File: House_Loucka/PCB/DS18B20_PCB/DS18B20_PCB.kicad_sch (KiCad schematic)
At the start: 3 parts, among them U1 DS18B20, U2 DS18B20, U3 DS18B20

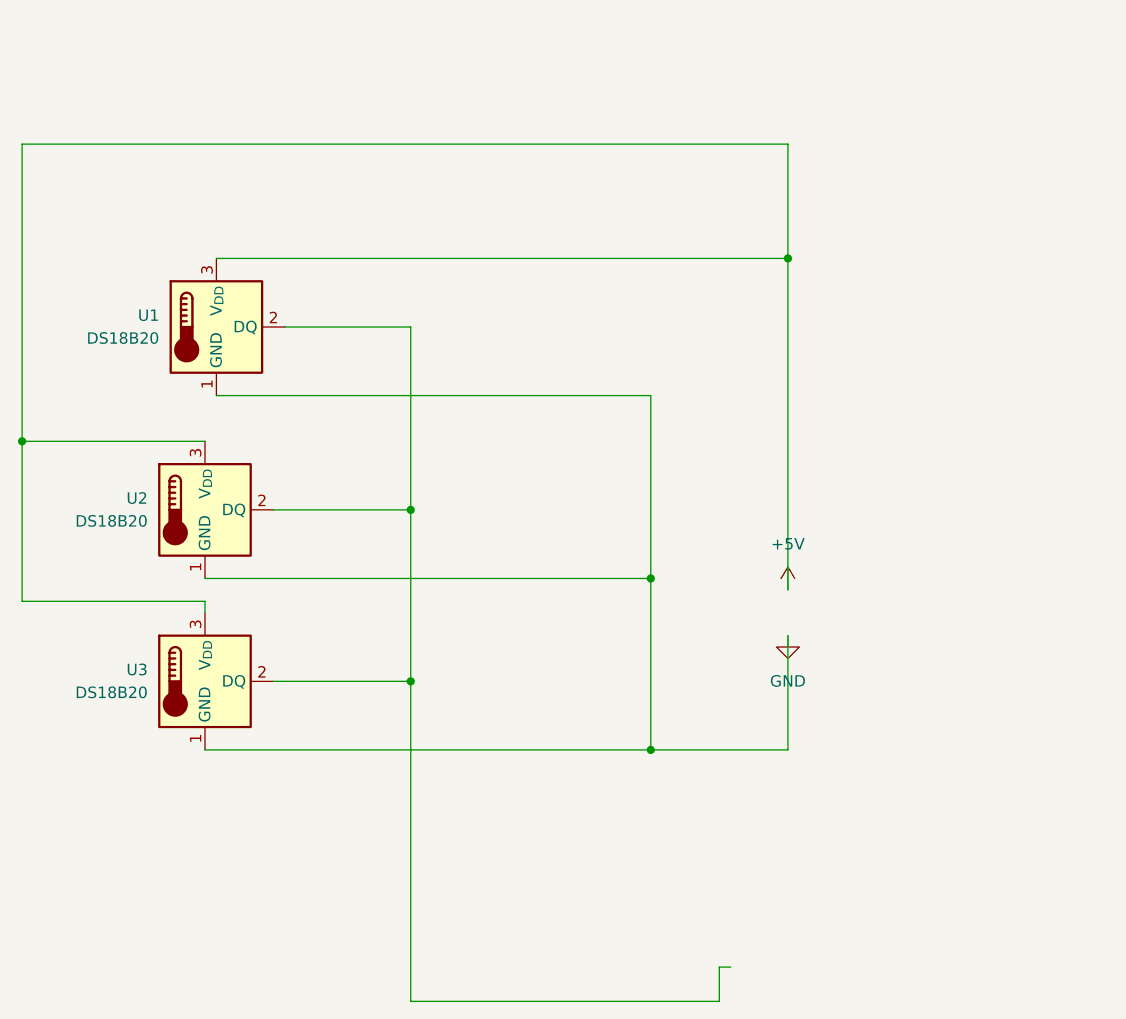
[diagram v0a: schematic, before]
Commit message: Update PCB DS18B20 tables updated
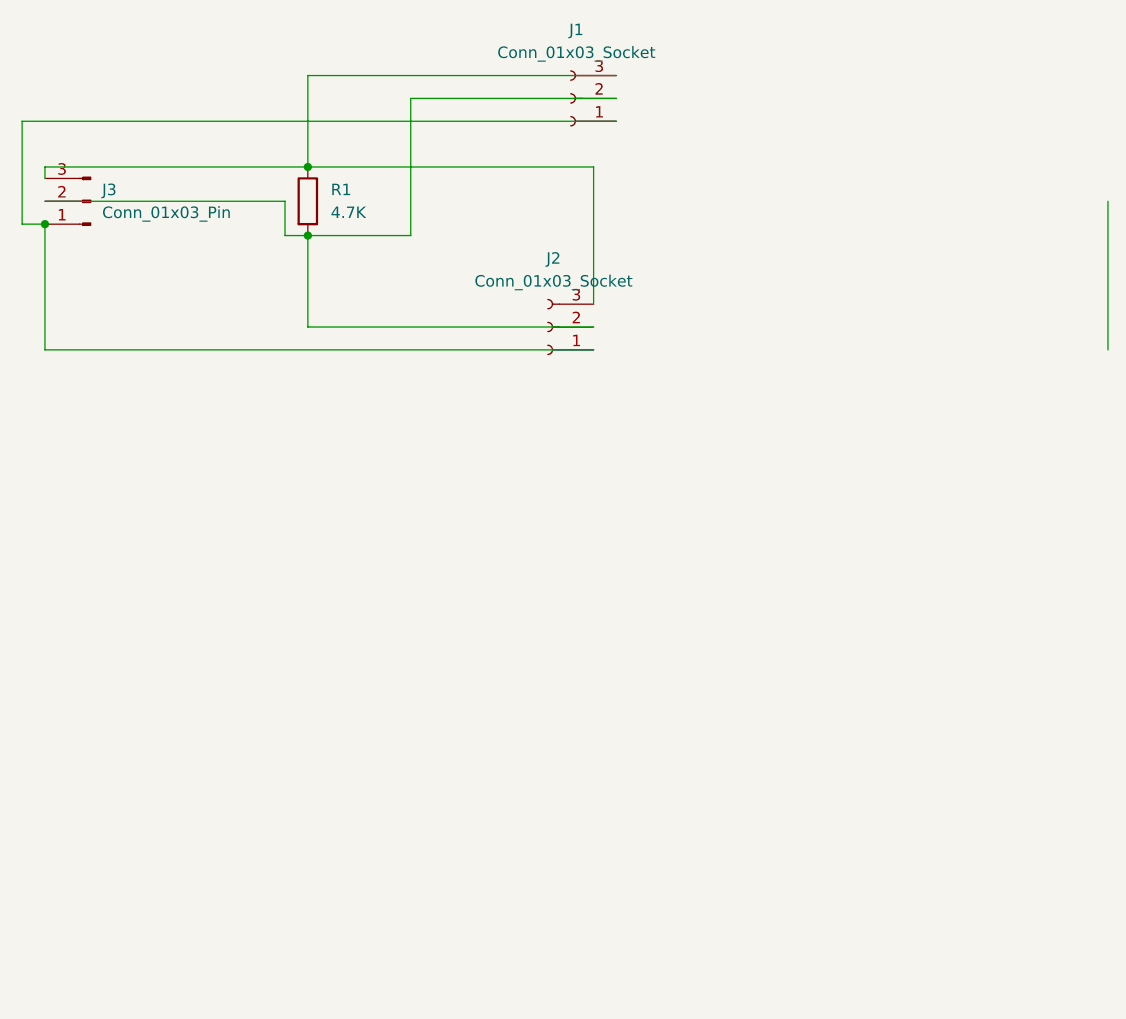
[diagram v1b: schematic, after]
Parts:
- removed U1, U2, U3: DS18B20, Package_TO_SOT_THT:TO-92_Inline, symbol Sensor_Temperature:DS18B20
- added J1, J2: Conn_01x03_Socket, Connector_PinSocket_2.54mm:PinSocket_1x03_P2.54mm_Vertical_SMD_Pin1Left, symbol Connector:Conn_01x03_Socket
- added J3: Conn_01x03_Pin, Connector_PinSocket_2.54mm:PinSocket_1x03_P2.54mm_Vertical_SMD_Pin1Right, symbol Connector:Conn_01x03_Pin
- added R1: 4.7K, Resistor_SMD:R_0201_0603Metric, symbol Device:R
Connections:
- new net: J1.1 (Pin_1), J2.1 (Pin_1), J3.1 (Pin_1)
- new net: J1.2 (Pin_2), J2.2 (Pin_2), J3.2 (Pin_2), R1.2
- new net: J1.3 (Pin_3), J2.3 (Pin_3), J3.3 (Pin_3), R1.1
